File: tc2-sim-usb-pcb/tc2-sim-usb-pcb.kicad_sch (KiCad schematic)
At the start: 9 parts, among them J501 Conn_01x08

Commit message: Fix library
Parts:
- J501: footprint Connector_PinHeader_2.54mm:PinHeader_1x08_P2.54mm_Vertical -> cacophony-library:Sim_connector
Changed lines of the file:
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@@
 			)
 		)
-		(property "Footprint" "Connector_PinHeader_2.54mm:PinHeader_1x08_P2.54mm_Vertical"
+		(property "Footprint" "cacophony-library:Sim_connector"
 			(at 236.22 130.81 0)
 			(hide yes)

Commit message: Add JLPCPCB 2D barcode to PCBs
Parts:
- added U504: (no value), cacophony-library:JLCPCB_QR_8mm, symbol cacophony-library:JLCPCB_QR_CODE
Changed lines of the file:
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@@
+	)
+	(symbol
+		(lib_id "cacophony-library:JLCPCB_QR_CODE")
+		(at 59.69 135.89 0)
+		(unit 1)
+		(body_style 1)
+		(exclude_from_sim yes)
+		(in_bom no)
+		(on_board yes)
+		(in_pos_files no)
+		(dnp no)
+		(fields_autoplaced yes)
+		(property "Reference" "U504"
+			(at 63.5 135.8899 0)
+			(show_name no)
+			(do_not_autoplace no)
+			(effects
+				(font
+					(size 1.27 1.27)
+				)
+				(justify left)
+			)
+		)
+		(property "Value" ""
+			(at 59.69 135.89 0)
+			(show_name no)
+			(do_not_autoplace no)
+			(effects
+				(font
+					(size 1.27 1.27)
+				)
+			)
+		)
+		(property "Footprint" "cacophony-library:JLCPCB_QR_8mm"
+			(at 59.69 135.89 0)
+			(hide yes)
+			(show_name no)
+			(do_not_autoplace no)
+			(effects
+				(font
+					(size 1.27 1.27)
+				)
+			)
+		)
+		(property "Datasheet" ""
+			(at 59.69 135.89 0)
+			(hide yes)
+			(show_name no)
+			(do_not_autoplace no)
+			(effects
+				(font
+					(size 1.27 1.27)
+				)
+			)
+		)
+		(property "Description" ""
+			(at 59.69 135.89 0)
+			(hide yes)
+			(show_name no)
+			(do_not_autoplace no)
+			(effects
+				(font
+					(size 1.27 1.27)
+				)
+			)
+		)
+		(instances
+			(project "tc2-sim-usb-pcb"
+				(path "/12797a05-1f89-472c-86ab-484e34ff8b5b"
+					(reference "U504")
+					(unit 1)
+				)
+			)
+		)
 	)
 	(symbol

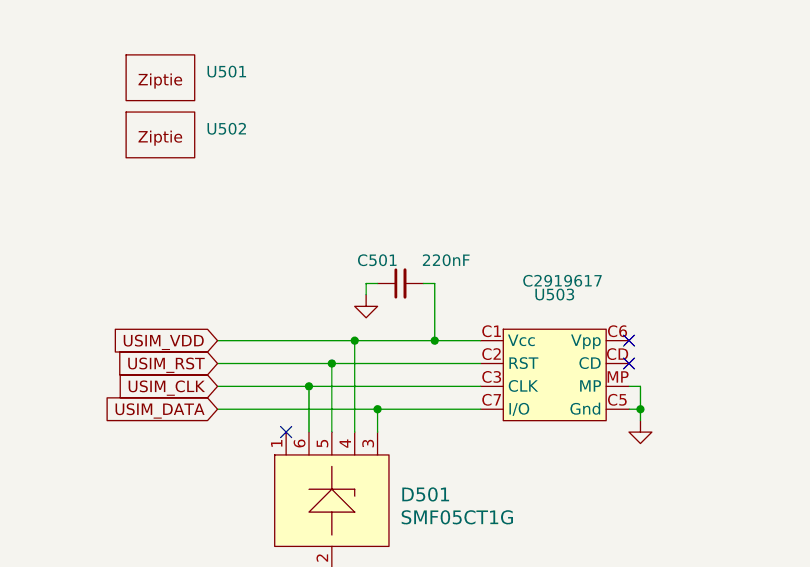
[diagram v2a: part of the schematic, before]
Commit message: Add git hash to PCBs
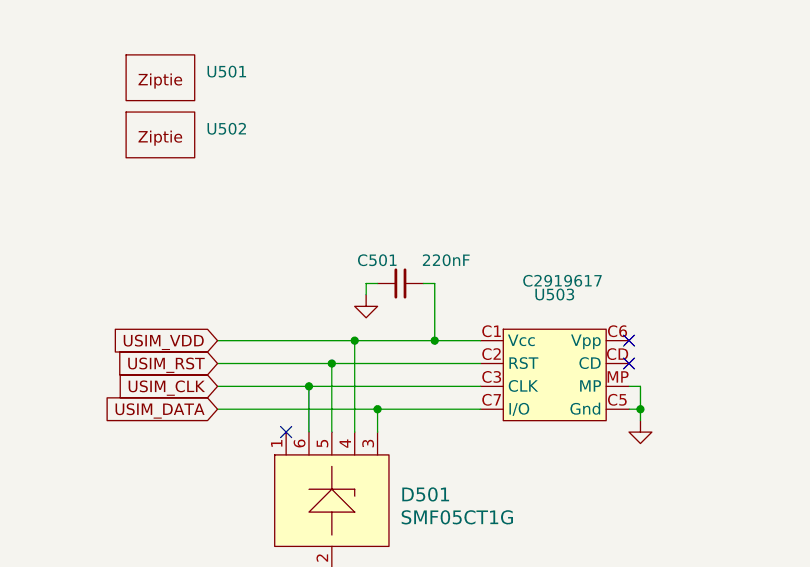
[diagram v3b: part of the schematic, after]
